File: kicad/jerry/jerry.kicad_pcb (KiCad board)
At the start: 2 copper layers, 33 parts, among them J1 Conn_01x06_Socket, U1 NE555P, U10 74LS08, U2 74LS393, U3 74HC595, U4 74LS266, U5 74HC74, U6 74HC04, U7 74LS21, U8 NE555P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

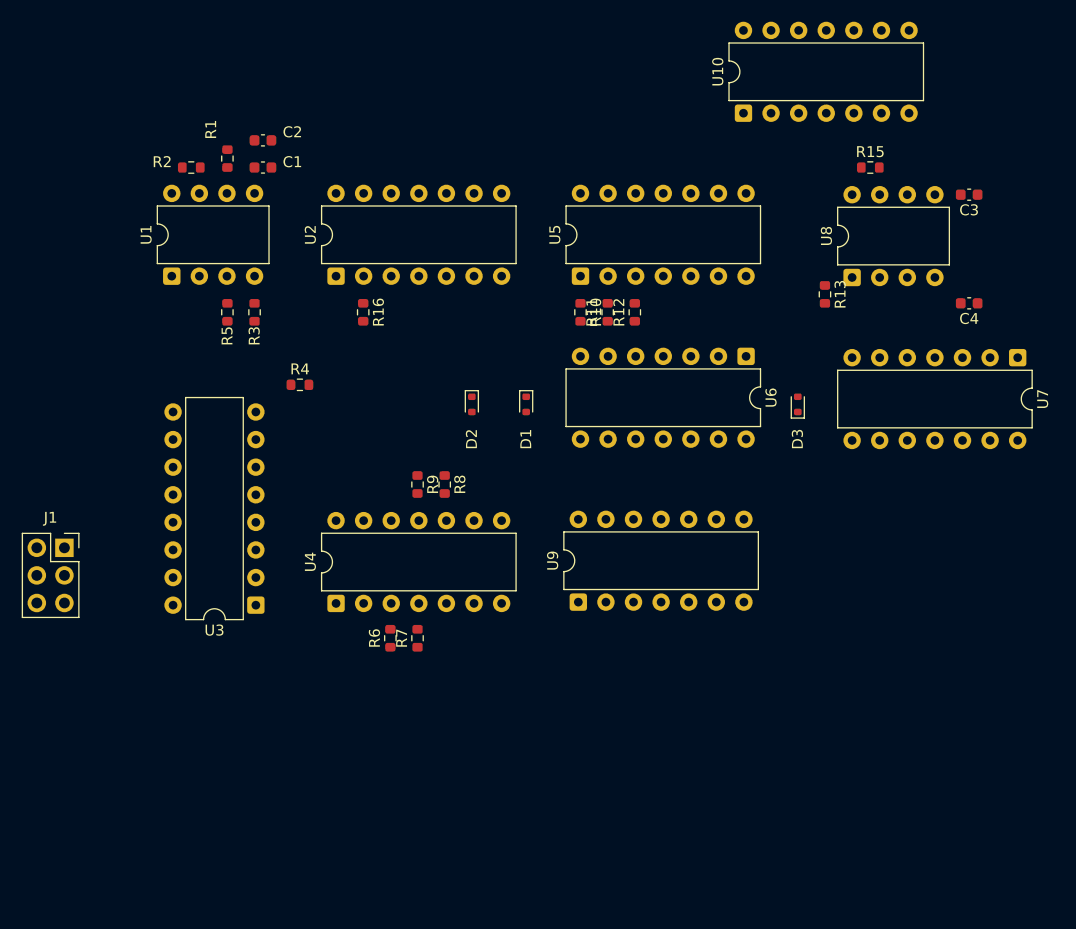
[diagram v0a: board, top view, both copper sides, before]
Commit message: updated pcb schematic
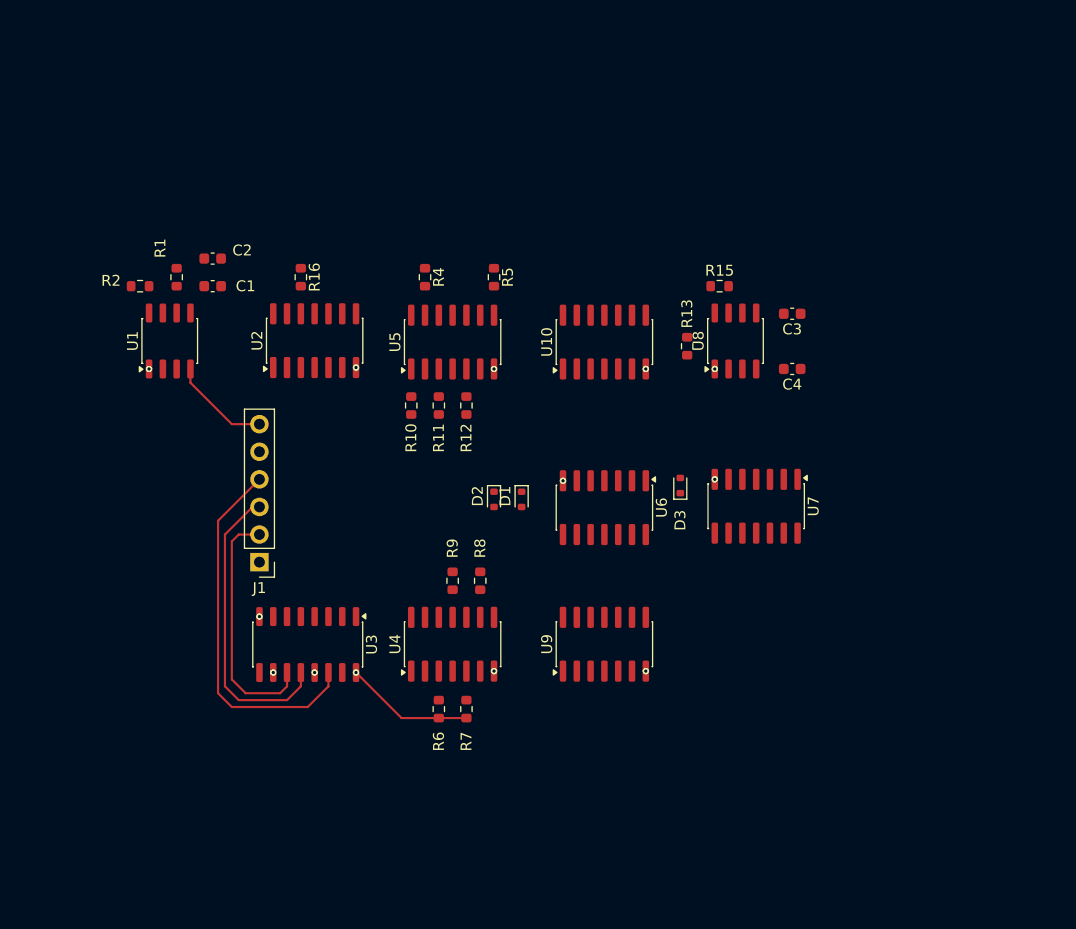
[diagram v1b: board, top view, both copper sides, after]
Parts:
- removed R3: 10k, Resistor_SMD:R_0603_1608Metric
- J1: footprint Connector_PinSocket_2.54mm:PinSocket_2x03_P2.54mm_Vertical -> Connector_PinHeader_2.54mm:PinHeader_1x06_P2.54mm_Vertical
- U1, U8: footprint Package_DIP:DIP-8_W7.62mm -> Package_SO:SO-8_3.9x4.9mm_P1.27mm
- U10, U2, U4, U5, U6, U7, U9: footprint Package_DIP:DIP-14_W7.62mm -> Package_SO:SO-14_3.9x8.65mm_P1.27mm
- U3: footprint Package_DIP:DIP-16_W7.62mm -> Package_SO:SO-16_3.9x9.9mm_P1.27mm
- moved U7 27.7 mm to (153.7, 78.7)
- moved R5 24.8 mm to (129.5, 57.6)
- moved U10 24.6 mm to (139.7, 63.6)
- moved C3 19.6 mm to (157.0, 61.0)
- moved U6 19.1 mm to (139.7, 78.8)
- moved J1 18.0 mm to (108.0, 83.8), turned to 180 degrees
- moved R10 17.8 mm to (121.9, 69.4)
- moved R11 17.8 mm to (124.5, 69.4)
- moved R12 17.7 mm to (127.0, 69.4)
- moved R15 17.7 mm to (150.3, 58.4)
- moved C4 17.4 mm to (157.0, 66.0)
- moved R4 15.2 mm to (123.2, 57.6), turned to -90 degrees
- moved R13 13.5 mm to (147.3, 63.9)
- moved U5 13.2 mm to (125.7, 63.6)
- moved D3 13.1 mm to (146.7, 76.8)
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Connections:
- J1 pad 2: OUT -> Net-(J1-Pin_2)
- J1 pad 5: Net-(J1-Pin_5) -> OUT
- U1 pad 4: Net-(U1-R) -> VCC
- U3 pad 11: Net-(J1-Pin_4) -> Net-(J1-Pin_2)
- U3 pad 14: Net-(J1-Pin_5) -> Net-(J1-Pin_4)
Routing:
- net Net-(J1-Pin_4): track 0.00 -> 34.0 mm
- net Net-(J1-Pin_3): track 0.00 -> 27.5 mm
- net Net-(J1-Pin_2): track 0.00 -> 22.6 mm
- net VCC: track 0.00 -> 21.1 mm, vias 0 -> 2
- net GND: vias 0 -> 11

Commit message: Redesigned pcb layout
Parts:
- C3, C4, R13, R15, U8: moved to B.Cu
- moved R5 52.9 mm to (129.1, 110.5), turned to 180 degrees
- moved R15 51.1 mm to (137.6, 108.0)
- moved R4 46.9 mm to (129.1, 104.1), turned to 180 degrees
- moved C3 46.2 mm to (144.3, 105.4)
- moved U5 43.2 mm to (123.1, 106.7), turned to 0 degrees
- moved U10 43.1 mm to (139.6, 106.7), turned to 0 degrees
- moved U8 41.4 mm to (139.1, 102.9), turned to -90 degrees
- moved R13 40.5 mm to (134.6, 102.4), turned to 90 degrees
- moved R16 40.3 mm to (129.1, 94.0), turned to 0 degrees
- moved R12 39.8 mm to (117.3, 108.0), turned to 0 degrees
- moved R11 36.7 mm to (117.3, 105.4), turned to 0 degrees
- moved C4 36.6 mm to (144.3, 100.3)
- moved U9 36.5 mm to (106.6, 106.7), turned to 0 degrees
- moved R10 33.8 mm to (117.3, 102.9), turned to 180 degrees
- moved U2 33.4 mm to (123.1, 95.2), turned to 0 degrees
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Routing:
- net Net-(J1-Pin_4): track 34.0 -> 0.00 mm
- net Net-(J1-Pin_3): track 27.5 -> 0.00 mm
- net Net-(J1-Pin_2): track 22.6 -> 0.00 mm
- net VCC: track 21.1 -> 31.8 mm, vias 2 -> 0
- net Net-(U1-DIS): track 0.00 -> 5.69 mm
- net /CONN: track 0.00 -> 4.03 mm
- net Net-(R6-Pad2): track 0.00 -> 3.06 mm
- net Net-(U1-CV): track 0.00 -> 3.00 mm
- net Net-(R7-Pad2): track 0.00 -> 2.80 mm
- net GND: track 0.00 -> 2.54 mm, vias 11 -> 4

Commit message: Finished custom routing. Needs cleanup.
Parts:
- moved R10 0.63 mm to (116.7, 102.9)
- moved R11 0.63 mm to (116.7, 105.4)
- moved R12 0.63 mm to (116.7, 108.0)
- moved C3 0.10 mm to (144.2, 105.5)
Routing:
- net VCC: track 31.8 -> 233.8 mm, vias 0 -> 3
- net Net-(U7-Pad13): track 0.00 -> 73.1 mm, vias 0 -> 2
- net GND: track 2.54 -> 65.9 mm, vias 4 -> 12
- net Net-(U2B-Q0): track 0.00 -> 57.8 mm
- net Net-(U5B-D): track 0.00 -> 49.2 mm, vias 0 -> 2
- net OUT: track 0.00 -> 48.5 mm, vias 0 -> 2
- net Net-(U5B-C): track 0.00 -> 36.2 mm, vias 0 -> 4
- net Net-(U2B-Q1): track 0.00 -> 34.5 mm, vias 0 -> 4
- net Net-(U5A-~{R}): track 0.00 -> 31.9 mm
- net /HIGH_BIT_RST: track 0.00 -> 31.7 mm, vias 0 -> 2
- net Net-(U2A-Q3): track 0.00 -> 24.2 mm, vias 0 -> 2
- net Net-(D1-K): track 0.00 -> 23.0 mm, vias 0 -> 3
- net /MS_CNTR_RST: track 0.00 -> 22.5 mm, vias 0 -> 3
- net Net-(R9-Pad2): track 0.00 -> 21.0 mm, vias 0 -> 2
- net Net-(U3-QC): track 0.00 -> 19.6 mm, vias 0 -> 2
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- added copper zone on B.Cu, net GND
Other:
- board outline added: 57.8 x 39.4 mm
